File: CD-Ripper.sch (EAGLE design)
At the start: 35 parts, among them IC1 MEGA48/88/168-PU, IC2 5V, K1 351, K2 JS-M1-12V-5, K3 351, K4 JS-M1-12V-5, Q1 20MHz, X1 MOTOR1, X2 MOTOR2, X3 USBPTH, X4 STATUS1, X5 STATUS2

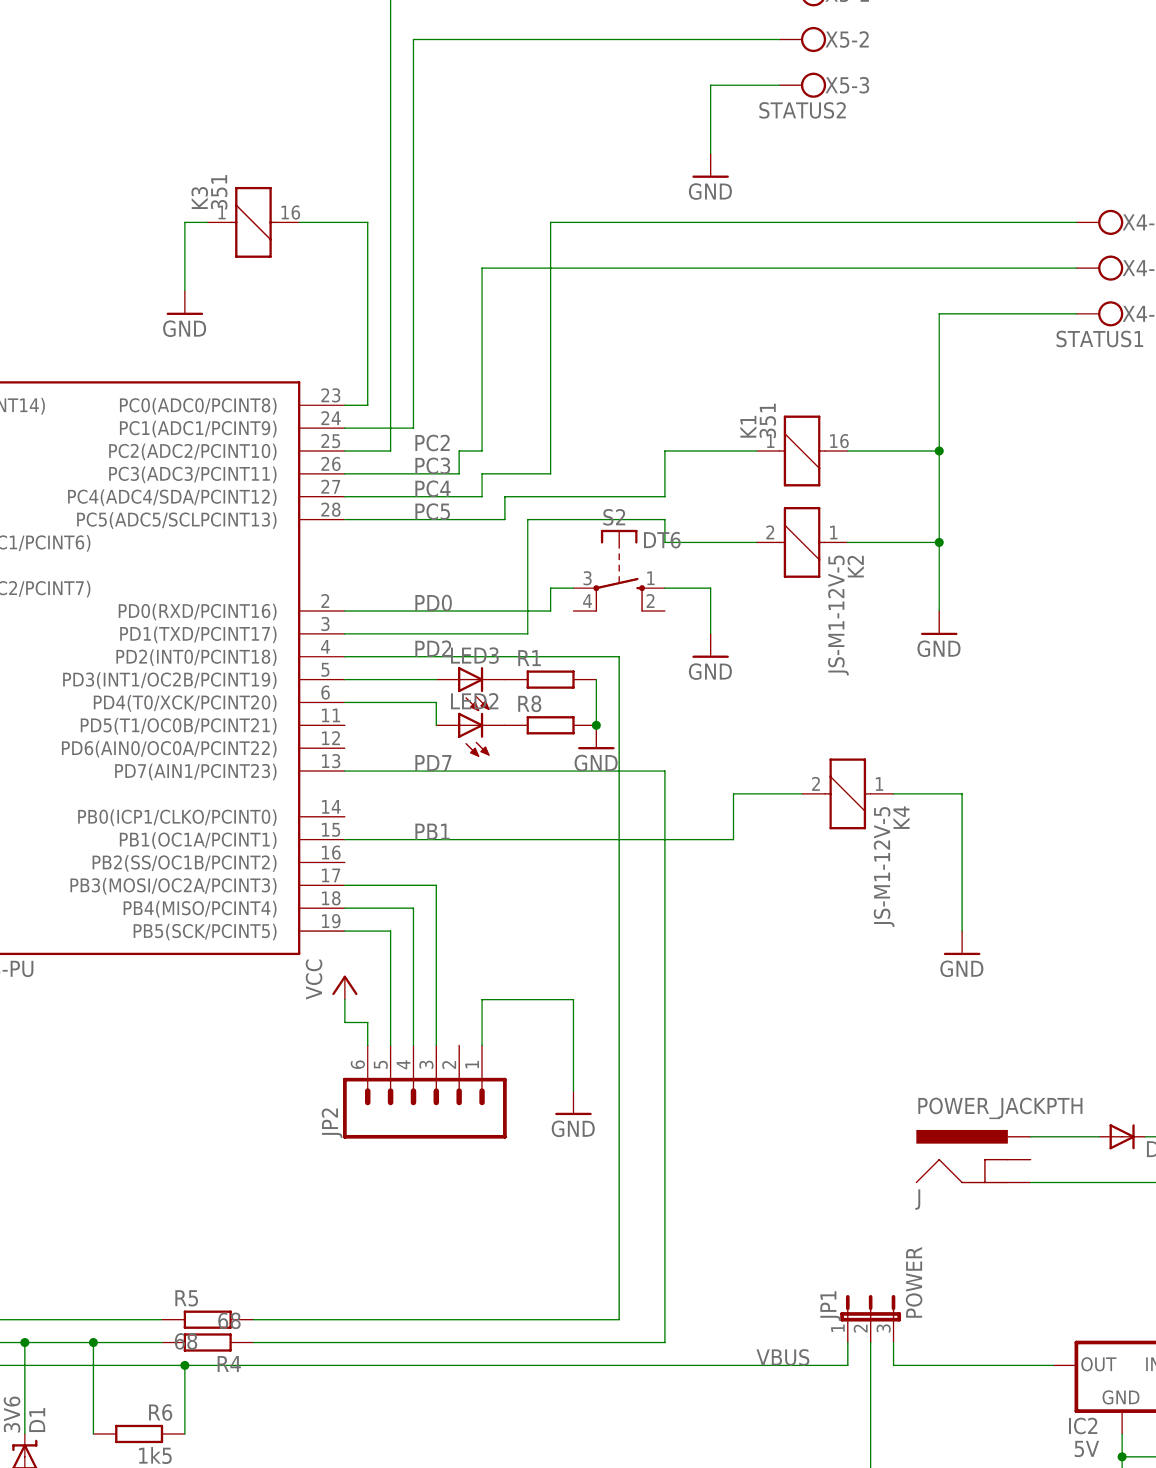
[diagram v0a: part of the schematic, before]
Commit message: Changed ICSP header.
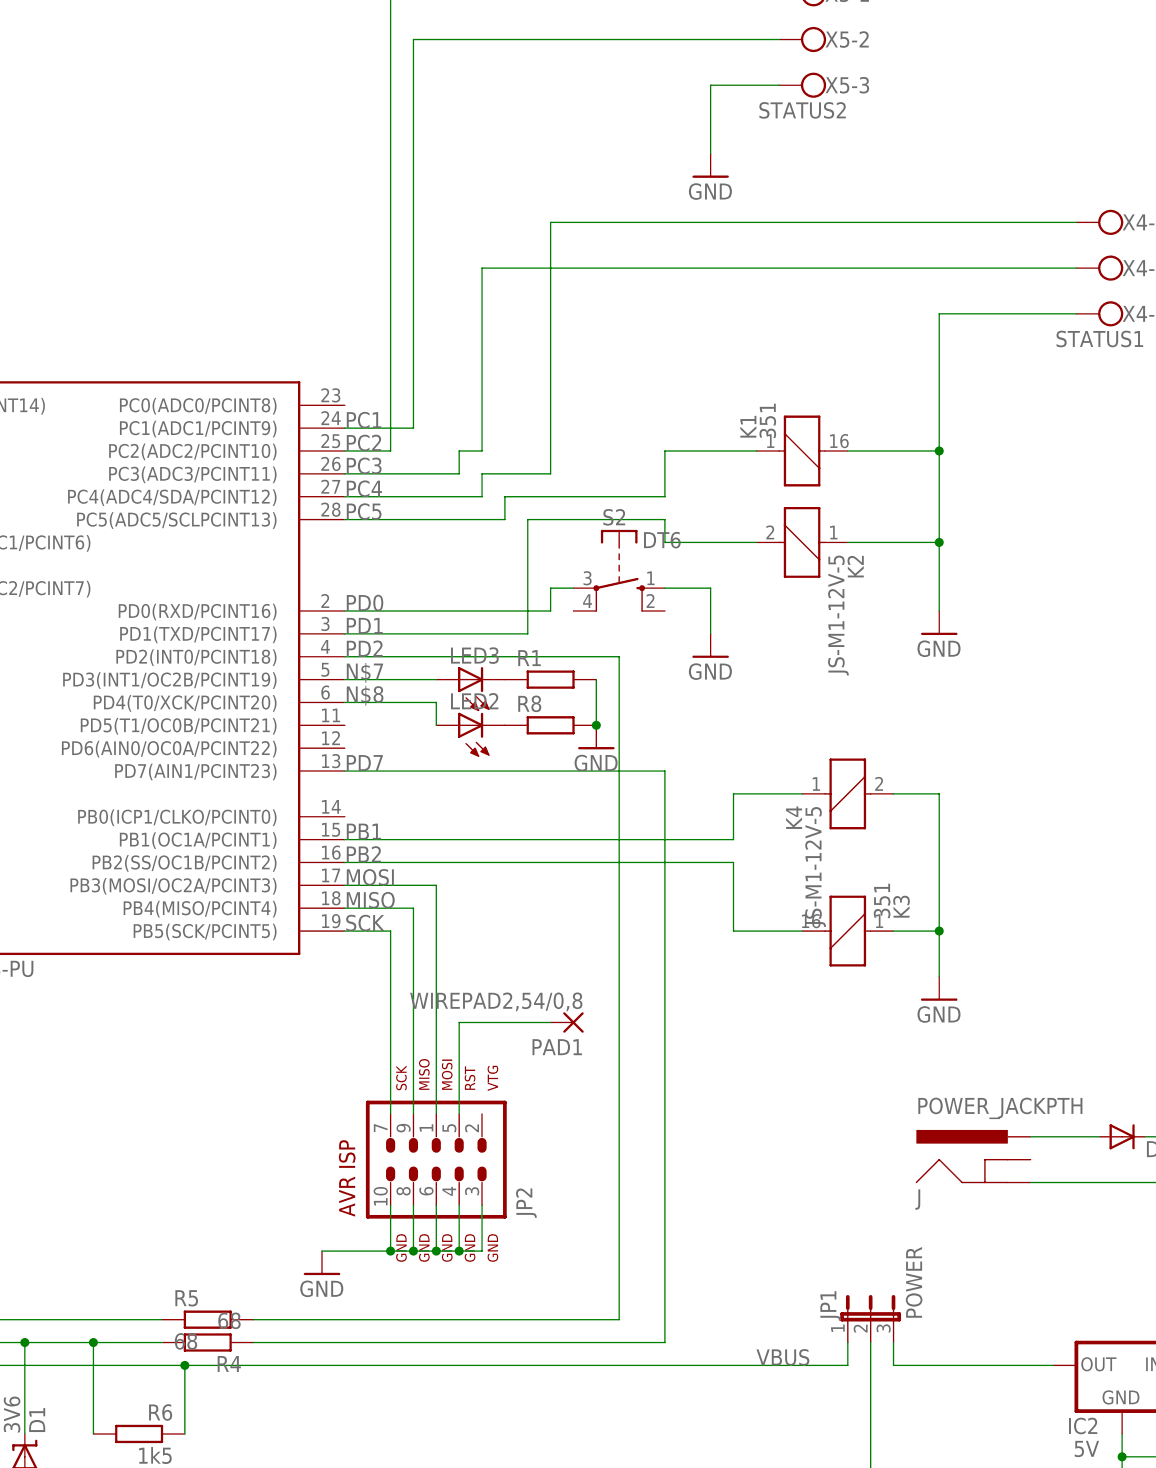
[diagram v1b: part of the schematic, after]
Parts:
- added PAD1: WIREPAD2,54/0,8, wirepad:WIREPAD2,54/0,8
- JP2: value (none) -> AVR-ISP-10; device SparkFun:M06SIP -> avr-7:AVR-ISP-10
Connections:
- net N$11 renamed PC1
- removed net N$15: IC1.PB5(SCK/PCINT5), JP2.5
- removed net N$16: IC1.PB4(MISO/PCINT4), JP2.4
- removed net N$17: IC1.PB3(MOSI/OC2A/PCINT3), JP2.3
- new net MISO: IC1.PB4(MISO/PCINT4), JP2.9
- new net MOSI: IC1.PB3(MOSI/OC2A/PCINT3), JP2.1
- new net PD1: IC1.PD1(TXD/PCINT17), K21.2
- new net SCK: IC1.PB5(SCK/PCINT5), JP2.7
- net GND: now also JP2.10, JP2.3, JP2.4, JP2.6, JP2.8, K41.2; no longer JP2.1, K41.1
- net N$10: now also JP2.5, PAD1.P; no longer IC1.PC2(ADC2/PCINT10), X5-1.KL
- net PB1: now also K41.1; no longer K41.2
- net PB2: now also IC1.PB2(SS/OC1B/PCINT2); no longer IC1.PC0(ADC0/PCINT8)
- net PC2: now also IC1.PC2(ADC2/PCINT10), X5-1.KL; no longer IC1.PC3(ADC3/PCINT11), X4-2.KL
- net PC3: now also IC1.PC3(ADC3/PCINT11), X4-2.KL; no longer IC1.PC4(ADC4/SDA/PCINT12), X4-1.KL
- net PC4: now also IC1.PC4(ADC4/SDA/PCINT12), X4-1.KL; no longer IC1.PC5(ADC5/SCLPCINT13), K11.1
- net PC5: now also IC1.PC5(ADC5/SCLPCINT13), K11.1; no longer IC1.PD1(TXD/PCINT17), K21.2
- net VCC: no longer JP2.6
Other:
- moved on the sheet: K3
